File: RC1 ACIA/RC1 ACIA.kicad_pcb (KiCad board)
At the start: 2 copper layers, 99.1 x 58.4 mm, 21 parts, among them J1 Expansion, J2 ADDRESS, J3 CONFIG, J4 FTDI, U1 R6551, U2 74LS00, U3 74LS138, U4 74LS138, X1 1.8432Mhz, Y1 1.8432Mhz

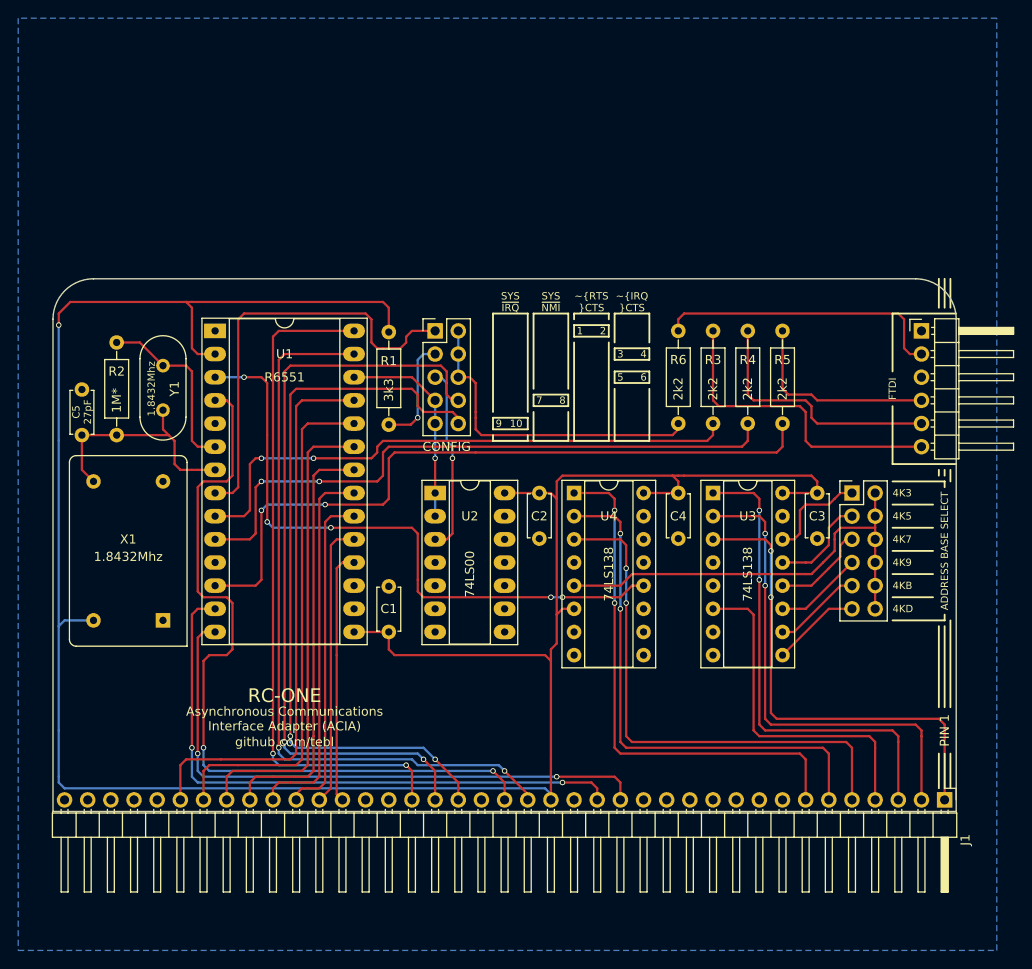
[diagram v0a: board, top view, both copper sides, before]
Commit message: Updated ACIA to make it work with external oscillator
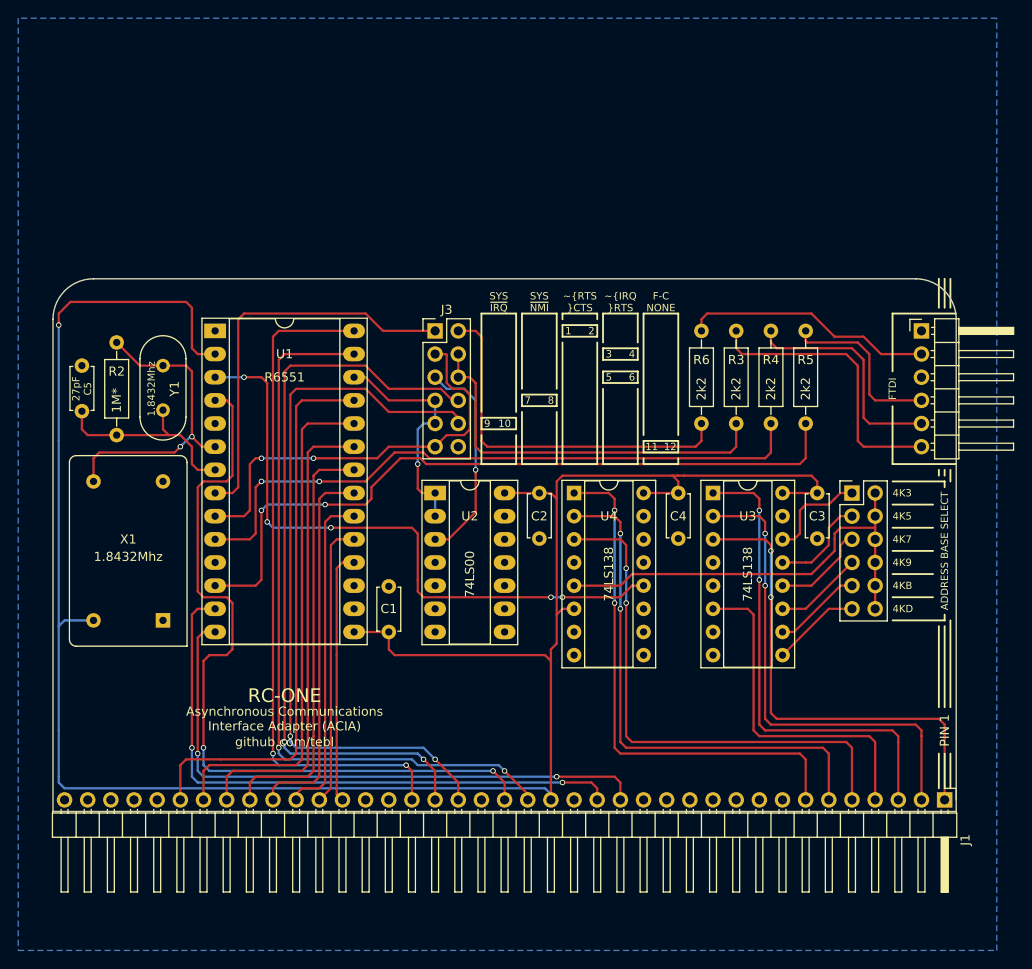
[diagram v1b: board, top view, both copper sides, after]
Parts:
- removed R1: 3k3, Resistors_THT:R_Axial_DIN0207_L6.3mm_D2.5mm_P10.16mm_Horizontal
- J3: footprint Pin_Headers:Pin_Header_Straight_2x05_Pitch2.54mm -> Pin_Headers:Pin_Header_Straight_2x06_Pitch2.54mm
- moved C5 7.62 mm to (98.4, 99.7), turned to 270 degrees
- moved R3 2.54 mm to (170.2, 106.0)
- moved R4 2.54 mm to (174.0, 106.0)
- moved R5 2.54 mm to (177.8, 106.0)
- moved R6 2.54 mm to (166.4, 106.0)
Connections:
- C5 pad 1: Net-(C5-Pad1) -> GND
- C5 pad 2: GND -> Net-(C5-Pad2)
- J3 pad 3: Net-(J3-Pad3) -> Net-(J3-Pad11)
- J3 pad 4: Net-(J3-Pad2) -> Net-(J3-Pad4)
- J3 pad 6: Net-(J3-Pad2) -> Net-(J3-Pad4)
- R2 pad 2: Net-(C5-Pad1) -> Net-(C5-Pad2)
- R3 pad 1: /~CTS -> Net-(J3-Pad4)
- U1 pad 7: Net-(C5-Pad1) -> Net-(C5-Pad2)
- U1 pad 9: /~CTS -> Net-(J3-Pad11)
- X1 pad 8: Net-(C5-Pad1) -> Net-(R2-Pad1)
- Y1 pad 2: Net-(C5-Pad1) -> Net-(C5-Pad2)
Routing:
- net /~CTS: track 62.9 -> 0.00 mm, vias 2 -> 0
- net Net-(J3-Pad11): track 0.00 -> 46.1 mm, vias 0 -> 2
- net Net-(J3-Pad4): track 0.00 -> 43.3 mm
- net Net-(C5-Pad1): track 26.3 -> 0.00 mm
- net VCC: track 267.2 -> 242.1 mm
- net Net-(C5-Pad2): track 0.00 -> 22.6 mm
- net Net-(R2-Pad1): track 20.0 -> 34.0 mm, vias 0 -> 2
- net Net-(J3-Pad3): track 12.6 -> 0.00 mm, vias 1 -> 0
- net Net-(J3-Pad2): track 35.7 -> 40.8 mm
- net Net-(J4-Pad2): track 31.9 -> 27.5 mm
- net Net-(J3-Pad1): track 47.3 -> 43.9 mm
- net Net-(J3-Pad7): track 22.6 -> 25.8 mm
- net Net-(J4-Pad4): track 22.1 -> 19.1 mm
- net Net-(J3-Pad5): track 20.5 -> 23.4 mm
- net Net-(J4-Pad5): track 28.1 -> 25.2 mm
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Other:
- board text added: "11"
- board text added: "12"
- board text added: "F-C NONE"
- board text added: "~IRQ ~RTS"
- board text removed: "~IRQ ~CTS"
